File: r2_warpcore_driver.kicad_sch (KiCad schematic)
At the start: 40 parts, among them J1 Conn_01x04_Pin, J10 Screw_Terminal_01x02, J11 Conn_01x03_Pin, J13 Conn_01x14_Pin, J14 Conn_01x05_Pin, J2 Conn_01x03_Pin, J3 Conn_01x03_Pin, J4 Conn_01x04_Pin, J5 Screw_Terminal_01x04, J6 Conn_01x05_Pin, J7 Screw_Terminal_01x04, J8 Screw_Terminal_01x04, J9 Screw_Terminal_01x03, Q1 L8050QLT1G, Q2 L8050QLT1G, Q3 IRLB8721PBF, Q4 IRLB8721PBF, Q5 IRLB8721PBF, SW1 SW_Push, SW2 SW_Push, U1 ESP32-S3-MINI-1

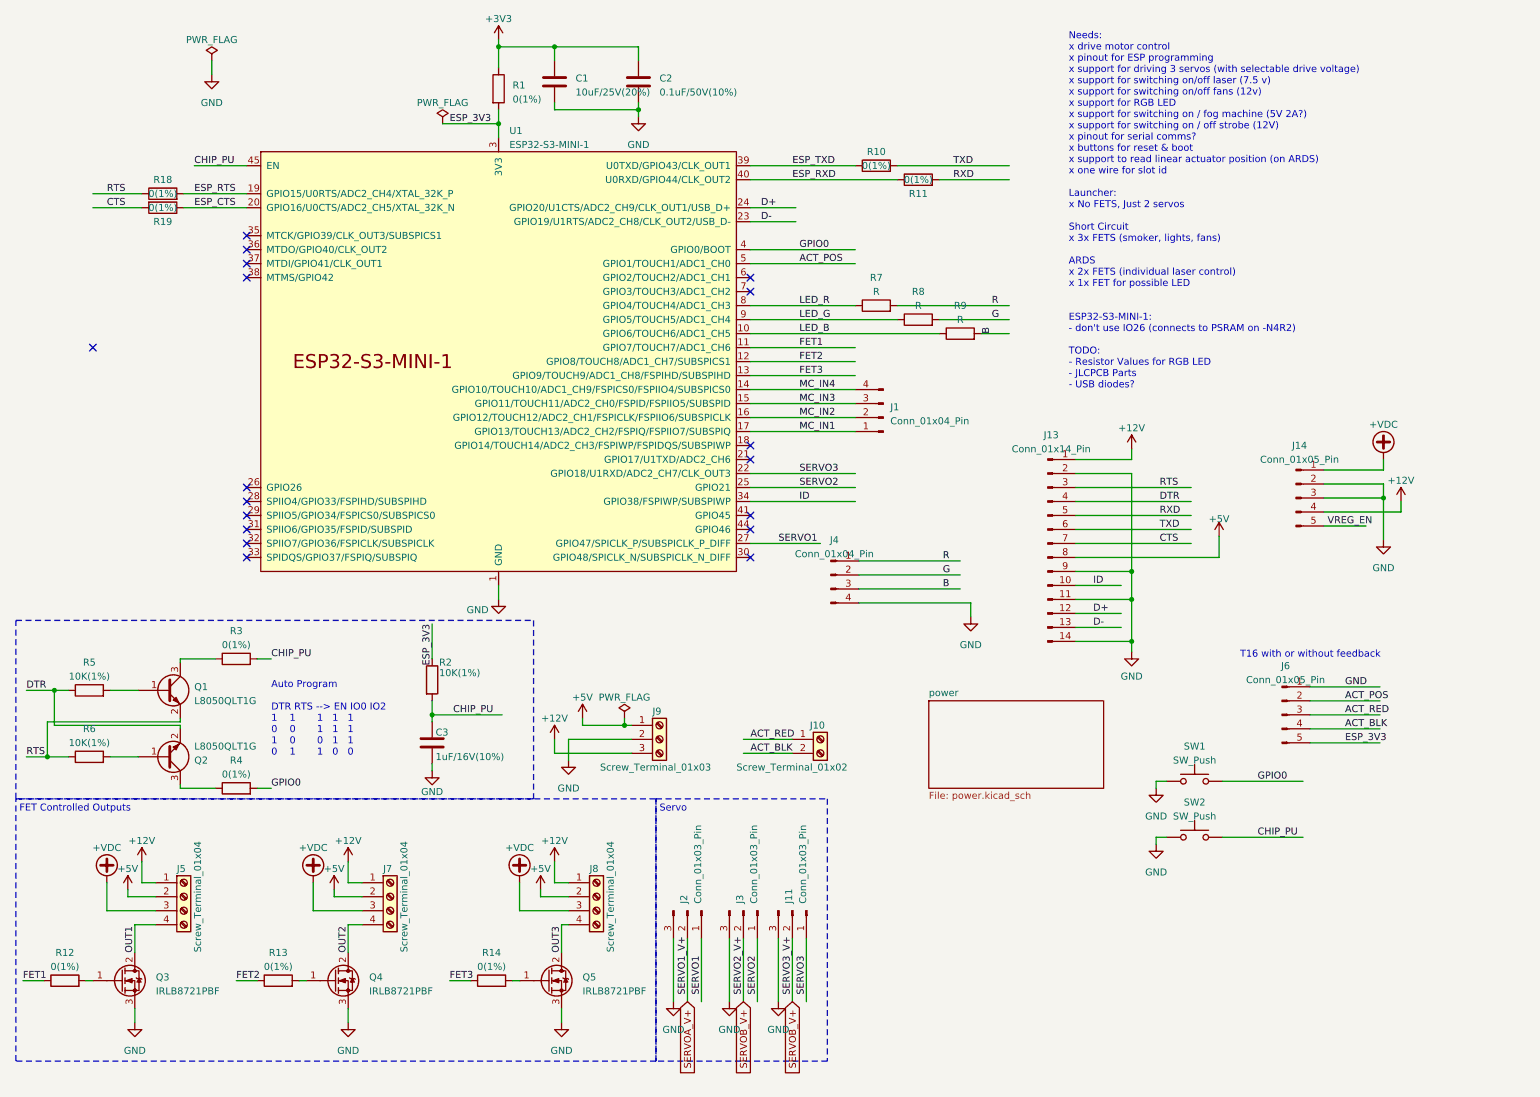
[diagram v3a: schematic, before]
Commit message: Updating JLC parts, adding transistor drive for RGB, USB diodes
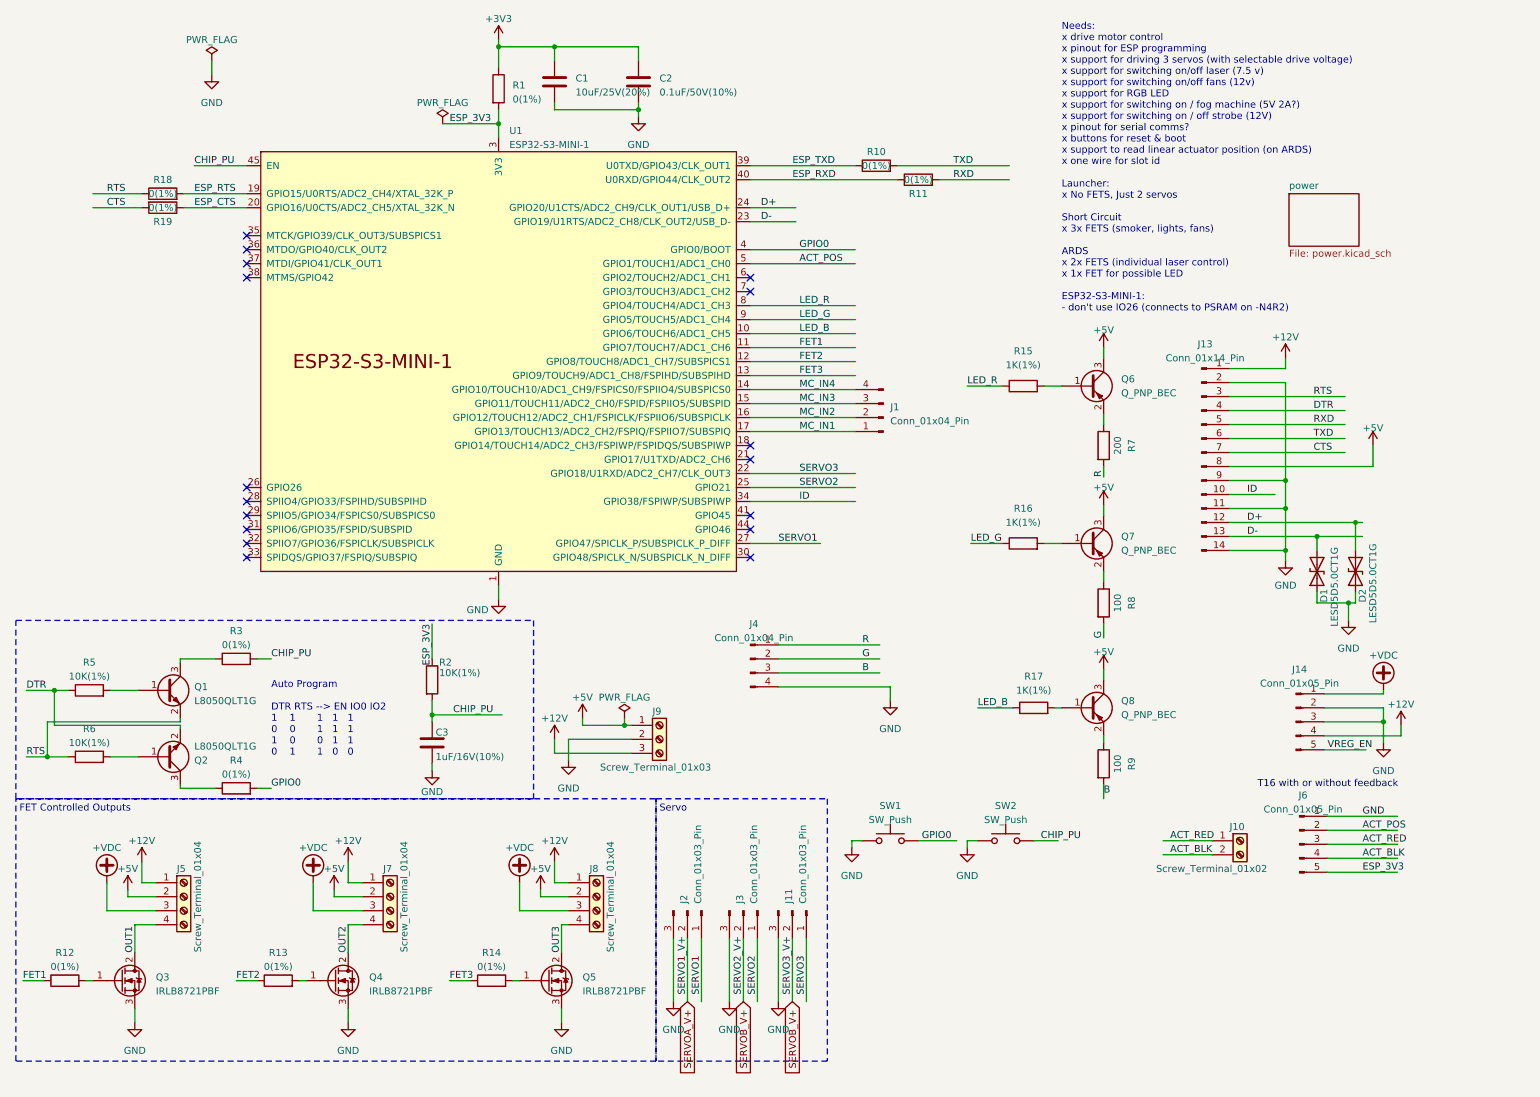
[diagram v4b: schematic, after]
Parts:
- added D1, D2: LESD5D5.0CT1G, Diode_SMD:D_SOD-523, symbol Device:D_TVS
- added Q6, Q7, Q8: Q_PNP_BEC, Package_TO_SOT_SMD:SOT-23-3, symbol Device:Q_PNP_BEC
- added R15, R16, R17: 1K(1%), Resistor_SMD:R_0402_1005Metric, symbol Device:R
- C1: footprint Capacitor_SMD:C_0402_1005Metric -> Capacitor_SMD:C_0805_2012Metric; JLCPCB (none) -> C15850
- C3: JLCPCB (none) -> C52923
- R7: value R -> 200; JLCPCB (none) -> C25087; Note (none) -> Should be 150ohm
- R8, R9: value R -> 100; JLCPCB (none) -> C25076
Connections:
- net +5V: now also Q6.3 (C), Q7.3 (C), Q8.3 (C)
- net D+: now also D2.2 (A2)
- net D-: now also D1.2 (A2)
- net GND: now also D1.1 (A1), D2.1 (A1)
- net LED_B: now also R17.1; no longer R9.1
- net LED_G: now also R16.1; no longer R8.1
- net LED_R: now also R15.1; no longer R7.1
- new net: Q6.2 (E), R7.1
- new net: Q8.2 (E), R9.1
- new net: Q8.1 (B), R17.2
- new net: Q7.1 (B), R16.2
- new net: Q7.2 (E), R8.1
- new net: Q6.1 (B), R15.2
- no-connect marks 18 -> 17
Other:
- moved on the sheet: J10, J13, J14, J4, J6, R9, SW1, SW2

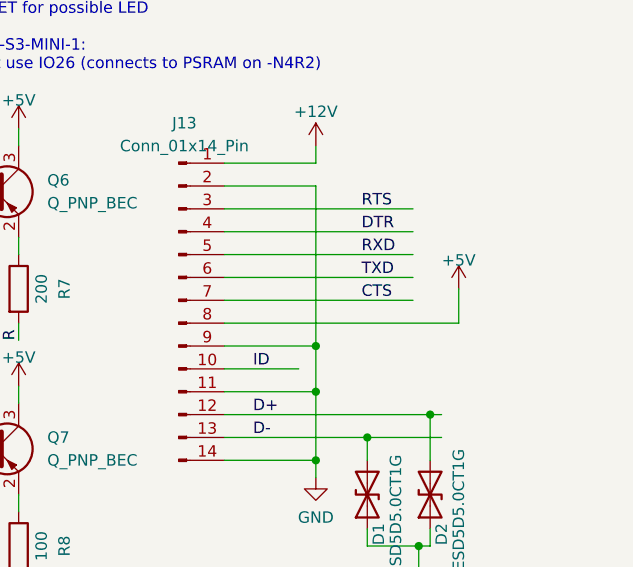
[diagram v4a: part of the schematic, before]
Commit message: Updates to set up USB traces, and to make it a 4-layer board.
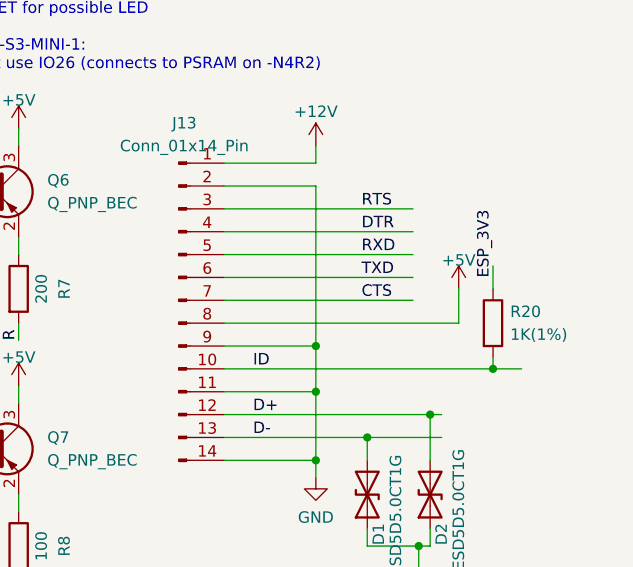
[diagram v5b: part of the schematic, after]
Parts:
- added R20: 1K(1%), Resistor_SMD:R_0402_1005Metric, symbol Device:R
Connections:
- net ESP_3V3: now also R20.1
- net ID: now also R20.2
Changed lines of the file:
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@@
   (junction (at 87.63 140.97) (diameter 0) (color 0 0 0 0)
+  )
+  (junction (at 262.255 100.965) (diameter 0) (color 0 0 0 0)
   )
   (junction (at 19.05 136.525) (diameter 0) (color 0 0 0 0)
@@
     (stroke (width 0) (type default))
   )
+  (wire (pts (xy 262.255 99.695) (xy 262.255 100.965))
+    (stroke (width 0) (type default))
+  )
   (wire (pts (xy 74.93 179.07) (xy 72.39 179.07))
     (stroke (width 0) (type default))
@@
     (stroke (width 0) (type default))
   )
+  (wire (pts (xy 262.255 100.965) (xy 265.43 100.965))
+    (stroke (width 0) (type default))
+  )
   (wire (pts (xy 209.55 144.78) (xy 209.55 146.05))
     (stroke (width 0) (type default))
@@
     (stroke (width 0) (type default))
   )
+  (wire (pts (xy 262.255 89.535) (xy 262.255 92.075))
+    (stroke (width 0) (type default))
+  )
   (wire (pts (xy 123.825 142.875) (xy 122.555 142.875))
     (stroke (width 0) (type default))
@@
     (stroke (width 0) (type default))
   )
-  (wire (pts (xy 232.41 100.965) (xy 240.665 100.965))
+  (wire (pts (xy 232.41 100.965) (xy 262.255 100.965))
     (stroke (width 0) (type default))
   )
@@
   )
   (label "CTS" (at 28.575 48.895 0) (fields_autoplaced)
+    (effects (font (size 1.27 1.27)) (justify left bottom))
+  )
+  (label "ESP_3V3" (at 262.255 90.805 90) (fields_autoplaced)
     (effects (font (size 1.27 1.27)) (justify left bottom))
   )
@@
     )
   )
+  (netclass_flag "" (length 2.54) (shape round) (at 153.035 51.435 0) (fields_autoplaced)
+    (effects (font (size 1.27 1.27)) (justify left bottom))
+    (property "Netclass" "USB Data" (at 153.7335 48.895 0)
+      (effects (font (size 1.27 1.27) italic) (justify left))
+    )
+  )
   (netclass_flag "" (length 2.54) (shape round) (at 240.665 78.105 0) (fields_autoplaced)
     (effects (font (size 1.27 1.27)) (justify left bottom))
     (property "Netclass" "High Current" (at 241.3635 75.565 0)
+      (effects (font (size 1.27 1.27) italic) (justify left))
+    )
+  )
+  (netclass_flag "" (length 2.54) (shape round) (at 151.765 48.895 0) (fields_autoplaced)
+    (effects (font (size 1.27 1.27)) (justify left bottom))
+    (property "Netclass" "USB Data" (at 152.4635 46.355 0)
       (effects (font (size 1.27 1.27) italic) (justify left))
     )
@@
         )
       )
+    )
+  )
+  (symbol (lib_id "Device:R") (at 262.255 95.885 0) (unit 1)
+    (in_bom yes) (on_board yes) (dnp no) (fields_autoplaced)
+    (property "Reference" "R20" (at 264.16 94.615 0)
+      (effects (font (size 1.27 1.27)) (justify left))
+    )
+    (property "Value" "1K(1%)" (at 264.16 97.155 0)
+      (effects (font (size 1.27 1.27)) (justify left))
+    )
+    (property "Footprint" "Resistor_SMD:R_0402_1005Metric" (at 260.477 95.885 90)
+      (effects (font (size 1.27 1.27)) hide)
+    )
+    (property "Datasheet" "https://jlcpcb.com/partdetail/12256-0402WGF1001TCE/C11702" (at 262.255 95.885 0)
+      (effects (font (size 1.27 1.27)) hide)
+    )
+    (property "JLCPCB" "C11702" (at 262.255 95.885 0)
+      (effects (font (size 1.27 1.27)) hide)
+    )
+    (pin "2")
+    (pin "1")
+    (instances
+      (project "r2_warpcore_driver"
+        (path "/6d80d172-24e2-4eb2-ae83-4ad814eadecf"
+          (reference "R20") (unit 1)
+        )
+      )

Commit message: Adding `JLCTYPE` to indicate `B` for Basic or `E` for Extended. Also attempts to output the necessary settings to populate headers.
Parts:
- C1, C2, C3, R1, R10, R11, R12, R13, R14, R15, R16, R17, R18, R19, R2, R20, R3, R4, R5, R6, R7, R8, R9: JLCTYPE (none) -> B
- D1, D2, Q3, Q4, Q5, SW1, SW2, U1: JLCTYPE (none) -> E
- Q1, Q2: JLCPCB C49581 -> C2146; JLCTYPE (none) -> B
- Q6, Q7, Q8: JLCPCB C127178 -> C105432; JLCTYPE (none) -> B

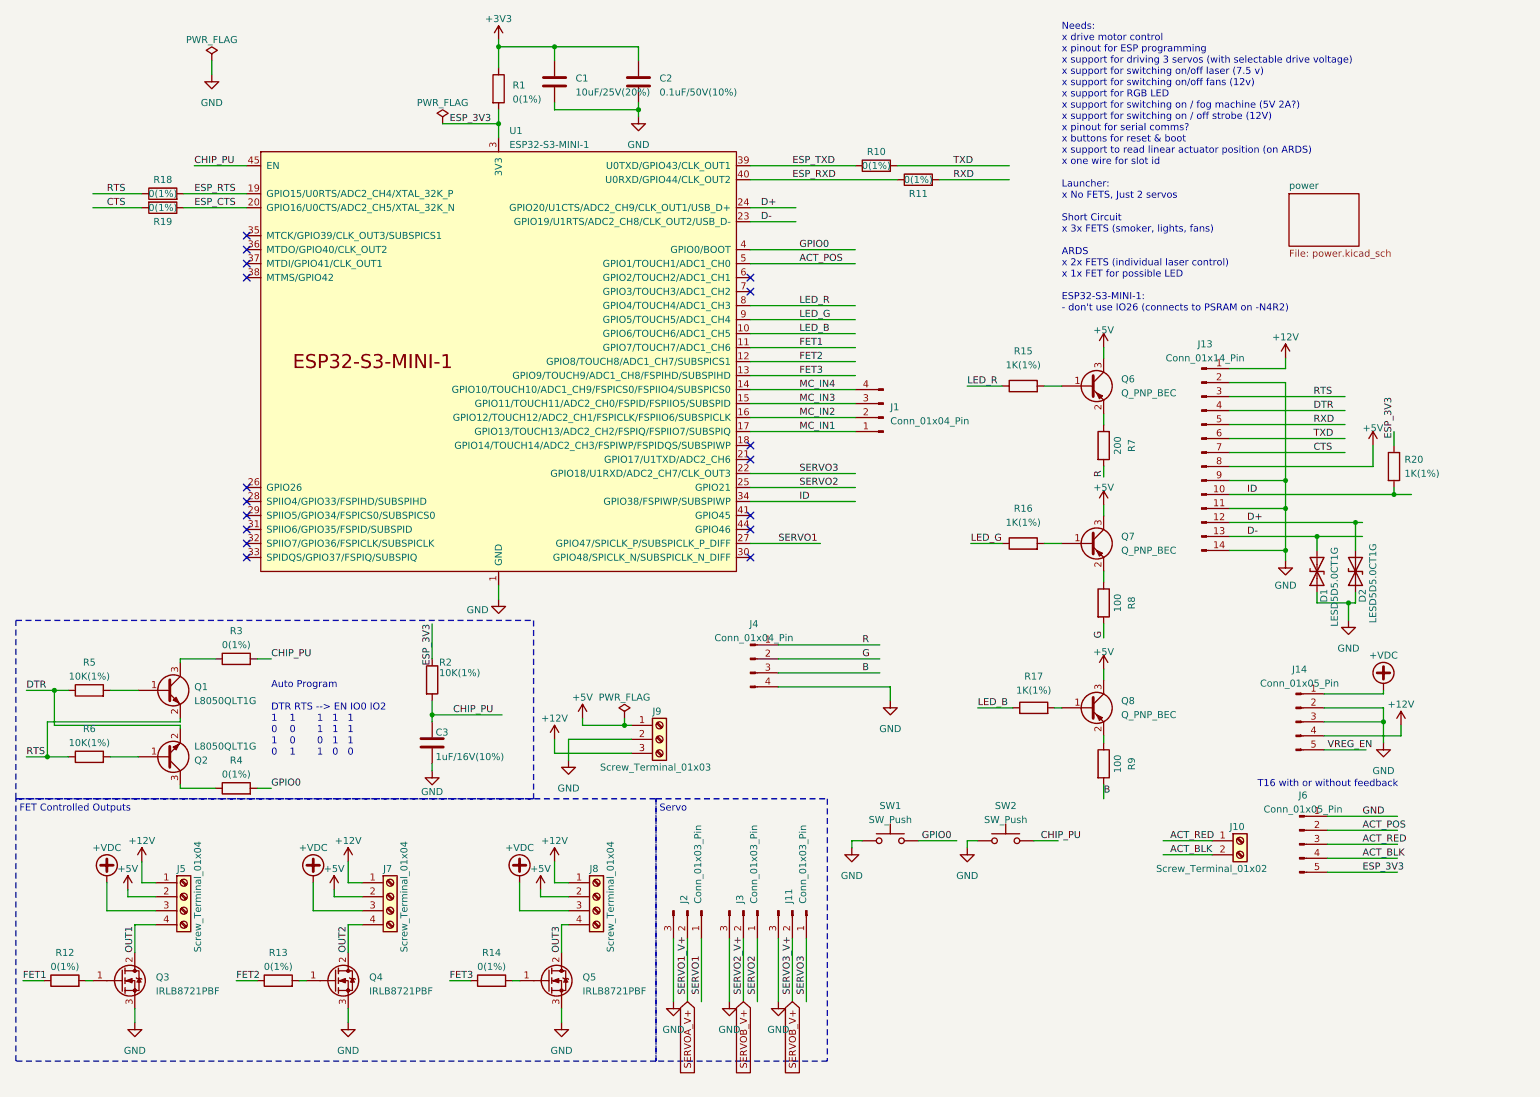
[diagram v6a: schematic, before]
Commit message: Updates to move to a USB socket.
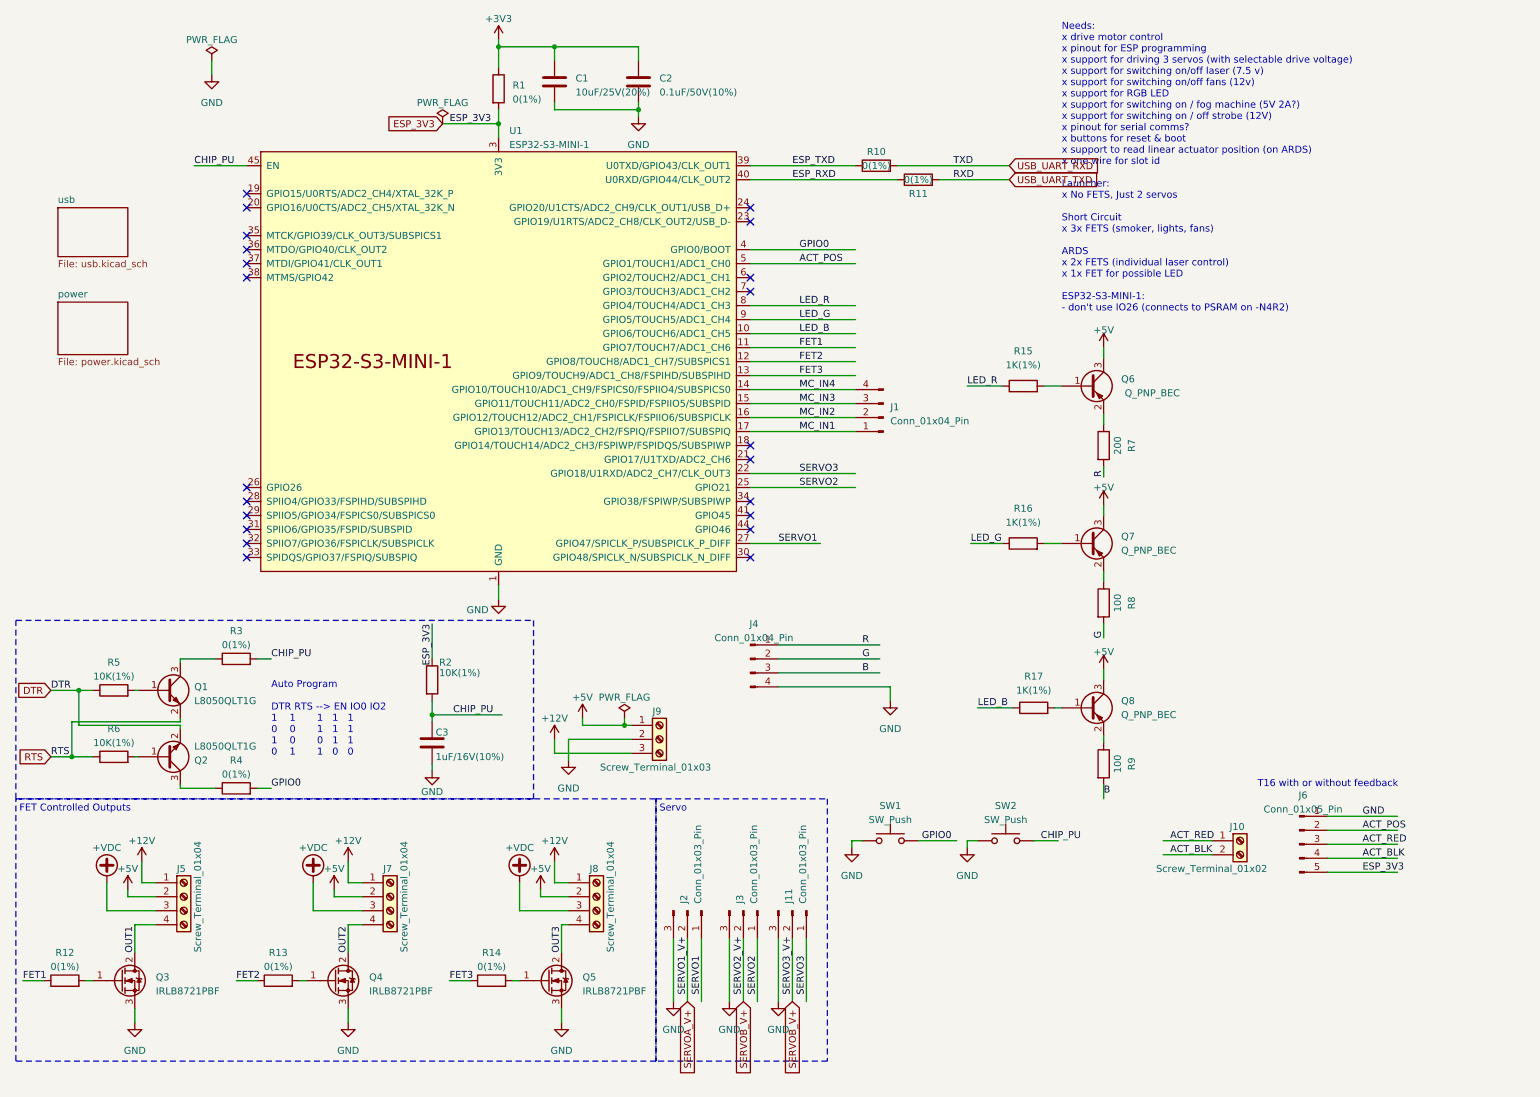
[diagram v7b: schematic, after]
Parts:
- removed D1, D2: LESD5D5.0CT1G, Diode_SMD:D_SOD-523, symbol Device:D_TVS
- removed J13: Conn_01x14_Pin, Connector_JST:JST_XH_B14B-XH-A_1x14_P2.50mm_Vertical, symbol Connector:Conn_01x14_Pin
- removed J14: Conn_01x05_Pin, Connector_PinHeader_2.54mm:PinHeader_1x05_P2.54mm_Vertical, symbol Connector:Conn_01x05_Pin
- removed R18, R19: 0(1%), Resistor_SMD:R_0402_1005Metric, symbol Device:R
- removed R20: 1K(1%), Resistor_SMD:R_0402_1005Metric, symbol Device:R
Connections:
- net D+: no longer names the net of U1.24 (GPIO20/U1CTS/ADC2_CH9/CLK_OUT1/USB_D+)
- net D-: no longer names the net of U1.23 (GPIO19/U1RTS/ADC2_CH8/CLK_OUT2/USB_D-)
- net ESP_CTS: no longer names the net of U1.20 (GPIO16/U0CTS/ADC2_CH5/XTAL_32K_N)
- net ESP_RTS: no longer names the net of U1.19 (GPIO15/U0RTS/ADC2_CH4/XTAL_32K_P)
- net ID: no longer names the net of U1.34 (GPIO38/FSPIWP/SUBSPIWP)
- net RXD renamed USB_UART_TXD
- net TXD renamed USB_UART_RXD
- no-connect marks 17 -> 22
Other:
- added sheet usb (usb.kicad_sch)
- moved on the sheet: R5, R6
